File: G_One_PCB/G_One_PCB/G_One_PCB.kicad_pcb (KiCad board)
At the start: 2 copper layers, 91 parts, among them K01(ESC)1 KEYSW, K02(F1)1 KEYSW, K03(F2)1 KEYSW, K04(F3)1 KEYSW, K05(F4)1 KEYSW, K07(F5)1 KEYSW, K10(M0)1 KEYSW, K11(_`_)1 KEYSW, K12(1!)1 KEYSW, K13(2@)1 KEYSW, K14(3#)1 KEYSW, K15(4$)1 KEYSW, K16(5%)1 KEYSW, K17(6^)1 KEYSW, K20(M1)1 KEYSW, K21(Tap)1 KEYSW, K22(Q)1 KEYSW, K23(W)1 KEYSW, K24(E)1 KEYSW, K25(R)1 KEYSW, K26(T)1 KEYSW, K27(P)1 KEYSW, K28(IoT0)1 KEYSW, K30(M2)1 KEYSW, K31(Caps_Lock)1 KEYSW, K32(A)1 KEYSW, K33(S)1 KEYSW, K34(D)1 KEYSW, K35(F)1 KEYSW, K36(G)1 KEYSW, K37(H)1 KEYSW, K38(IoT1)1 KEYSW, K40(M3)1 KEYSW, K41(L_Shift)1 KEYSW, K42(Z)1 KEYSW, K43(X)1 KEYSW, K44(C)1 KEYSW, K45(V)1 KEYSW, K46(B)1 KEYSW, K48(IoT2)1 KEYSW, K50(M4)1 KEYSW, K51(L_CTRL)1 KEYSW, K52(Win)1 KEYSW, K53(L_ALT)1 KEYSW, K54(Space)1 KEYSW

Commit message: pcb 수정
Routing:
- net /col7: track 95.2 -> 158.2 mm, vias 0 -> 2
- net /col0: track 262.2 -> 309.4 mm, vias 2 -> 0
- net /row5: track 263.5 -> 226.8 mm, vias 0 -> 6
- net /row1: track 204.3 -> 226.6 mm
- net /col4: track 235.0 -> 219.0 mm
- net /col5: track 193.6 -> 178.6 mm, vias 4 -> 2
- net /row3: track 256.4 -> 245.8 mm, vias 0 -> 2
- net /row4: track 270.9 -> 261.5 mm, vias 0 -> 2
- net /row0: track 171.7 -> 180.3 mm
- net /row2: track 236.9 -> 228.7 mm
- net /col1: track 289.9 -> 295.6 mm, vias 4 -> 0
- net /col6: track 140.3 -> 145.0 mm
- net /col3: track 255.5 -> 257.9 mm, vias 4 -> 0
- net /col2: track 278.4 -> 280.1 mm, vias 4 -> 0
- net /col8: track 52.0 -> 53.2 mm

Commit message: PCB 제작 완료 및 거버 파일 생성
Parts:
- added REF**: MountingHole_3.2mm_M3_Pad, MountingHole:MountingHole_3.2mm_M3_Pad, F.Cu at (215.1, -4.12)
- added REF**: MountingHole_3.2mm_M3_Pad, MountingHole:MountingHole_3.2mm_M3_Pad, F.Cu at (215.1, -129.6)
- added REF**: MountingHole_3.2mm_M3_Pad, MountingHole:MountingHole_3.2mm_M3_Pad, F.Cu at (4.12, -4.12)
- added REF**: MountingHole_3.2mm_M3_Pad, MountingHole:MountingHole_3.2mm_M3_Pad, F.Cu at (4.12, -129.6)
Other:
- board outline added: 219.2 x 133.8 mm

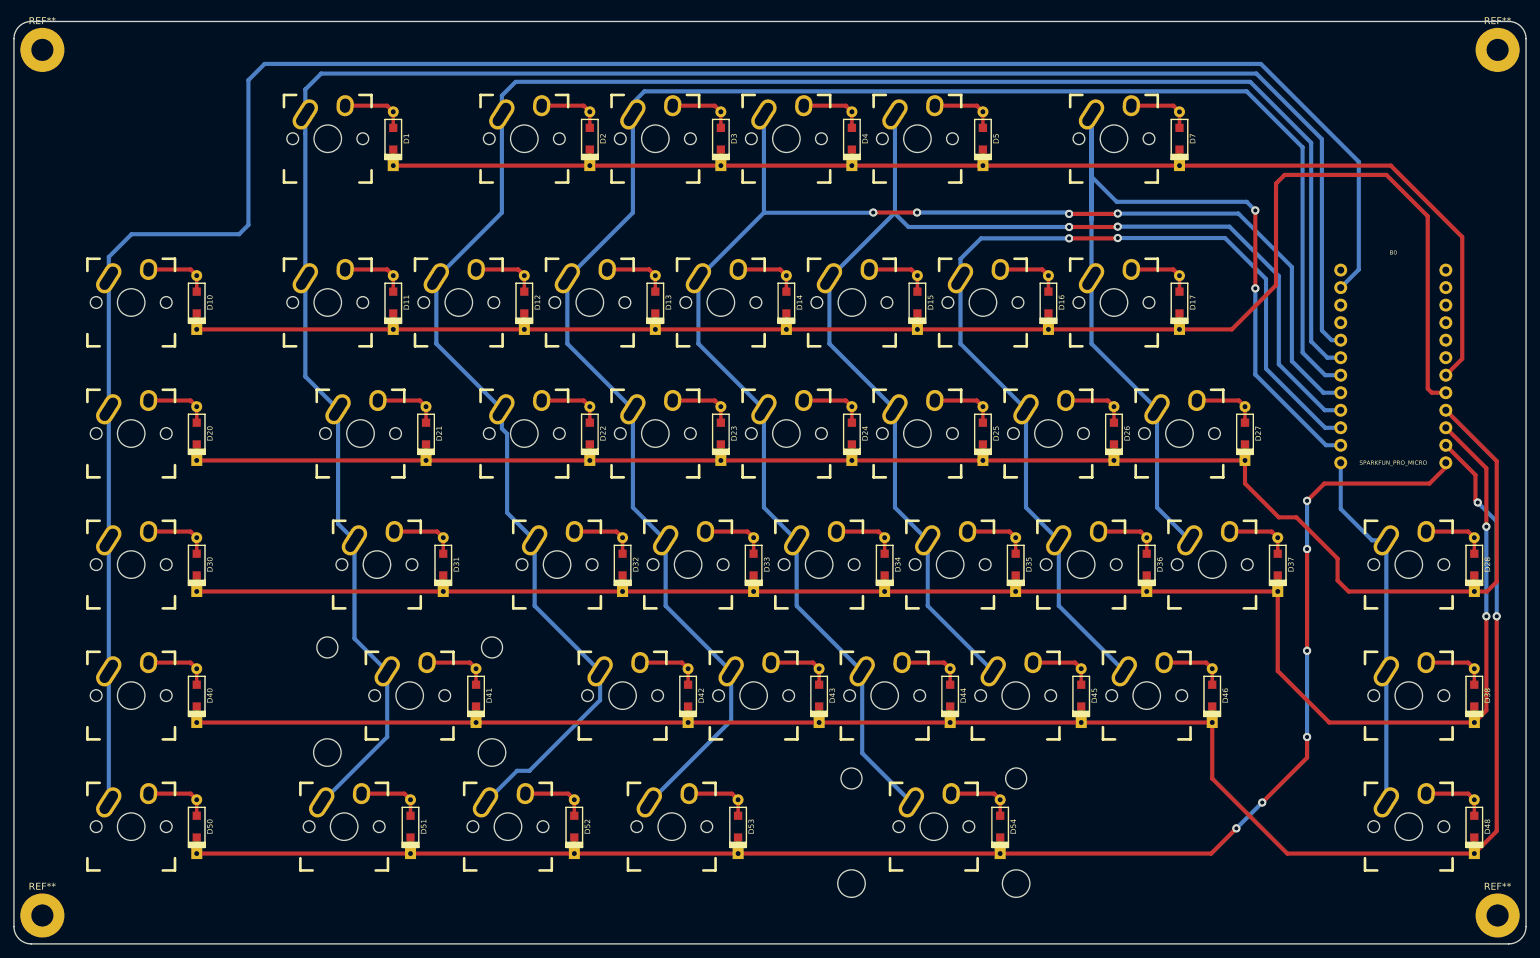
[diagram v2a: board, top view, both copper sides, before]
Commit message: 필요없는 파일 삭제
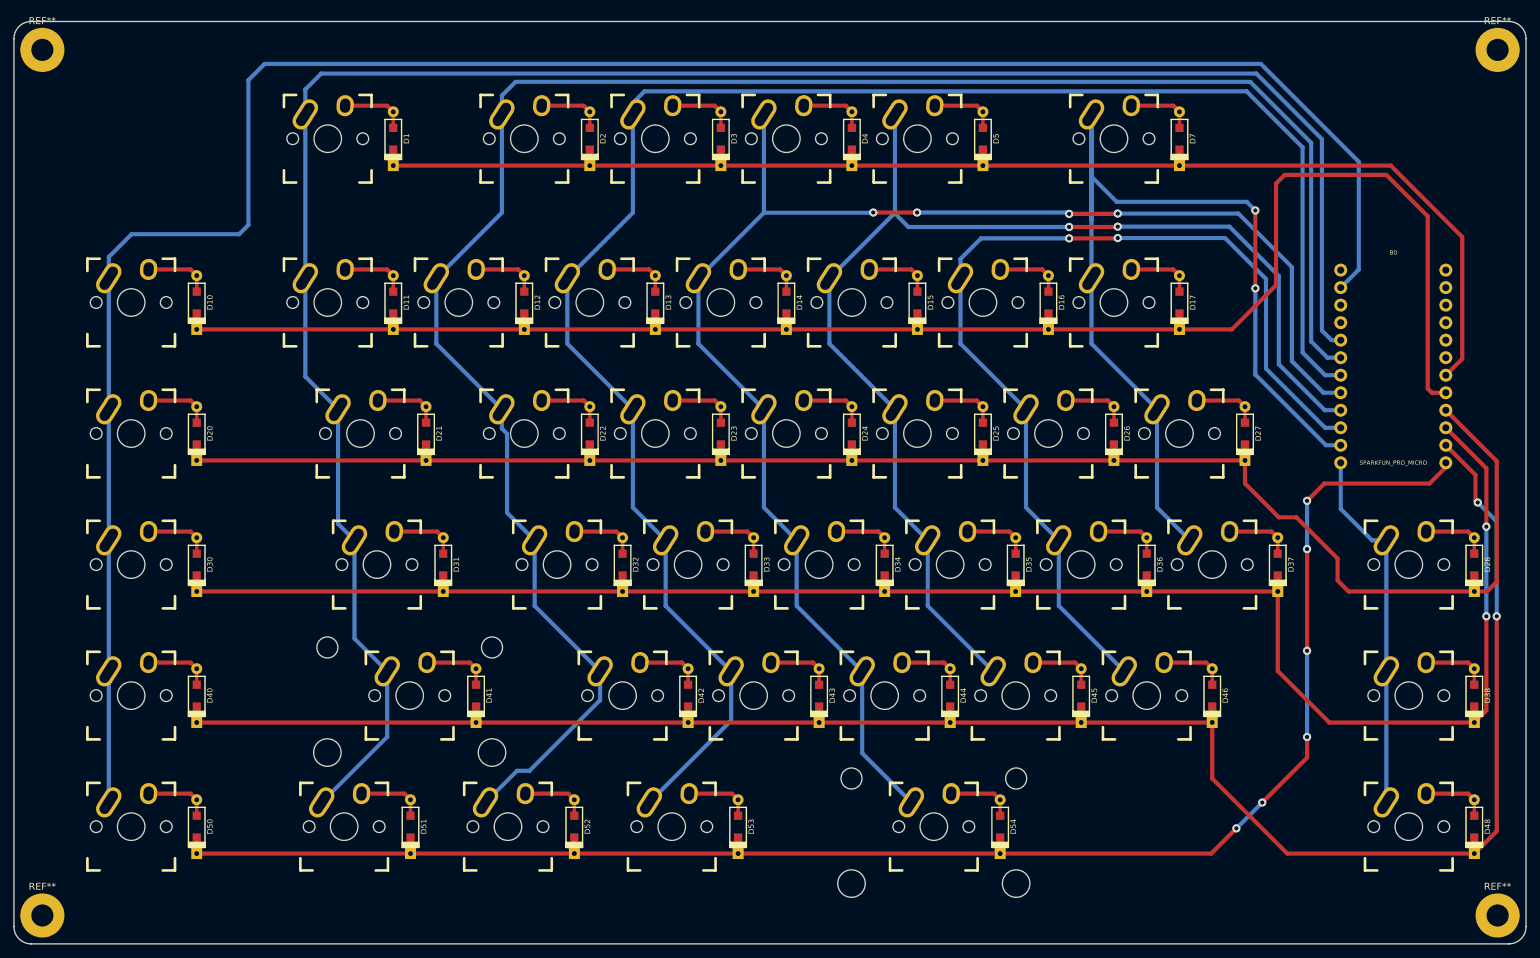
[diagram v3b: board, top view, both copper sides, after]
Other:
- net class Default removed
